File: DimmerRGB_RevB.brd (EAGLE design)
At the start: 75 x 65 mm, 61 parts, among them CON1 CON_10X200MIL, CON2 CON_5X100MIL, IC1 PIC16F18325, IC2 LM2931_ADJ, IC3 LM5111, IC4 LM5111, IC5 74HC14D, Q2 N-PWR-MOSFETLFPAK, Q3 N-PWR-MOSFETLFPAK, Q4 N-PWR-MOSFETLFPAK, Q5 N-PWR-MOSFETLFPAK, SW1 PEC11R, SW2 PEC11R, SW3 PEC09, SW4 PEC09

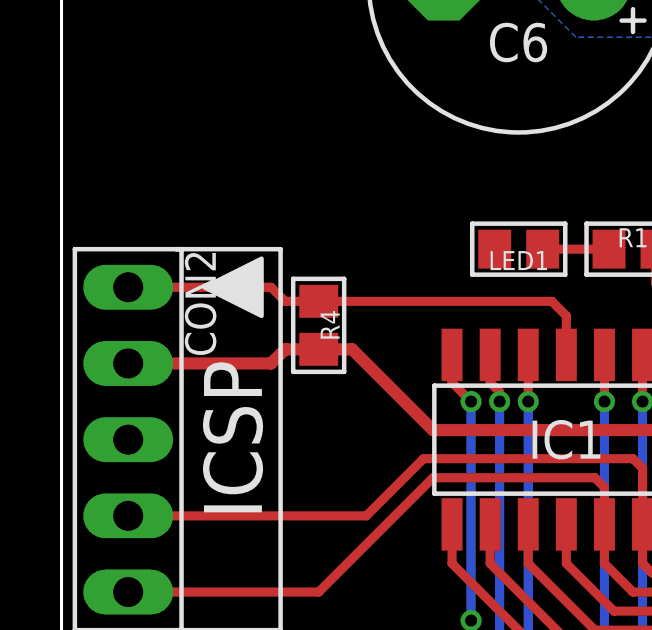
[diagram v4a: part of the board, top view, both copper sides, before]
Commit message: Linear regulator changed
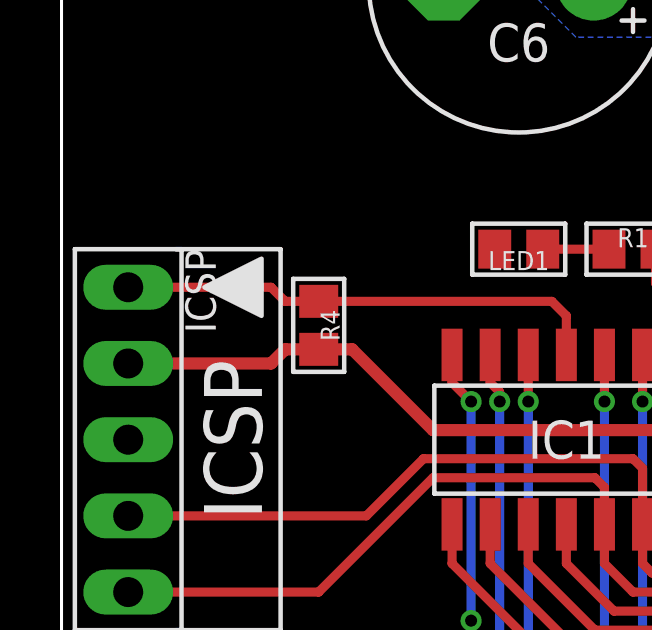
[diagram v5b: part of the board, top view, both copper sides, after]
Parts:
- C3, C4, C5, C6, C7: value 1500u -> 330u 35V
- IC2: value LM2931_ADJ -> LM2936
- IC3, IC4: value LM5111 -> LM5111-1M
- Q1: value (none) -> NX3008NBK
- R2: value 33k -> N/A
- R3: value 10k -> N/A
- R5: value 33k -> 22k
- renumbered CON2 to ICSP
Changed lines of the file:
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@@
 <layer number="25" name="tNames" color="7" fill="1" visible="no" active="yes"/>
 <layer number="26" name="bNames" color="7" fill="1" visible="no" active="yes"/>
-<layer number="27" name="tValues" color="7" fill="1" visible="no" active="yes"/>
+<layer number="27" name="tValues" color="7" fill="1" visible="yes" active="yes"/>
 <layer number="28" name="bValues" color="7" fill="1" visible="no" active="yes"/>
 <layer number="29" name="tStop" color="7" fill="3" visible="no" active="yes"/>
@@
 <element name="Q5" library="00Mosfet" package="LFPAK" value="N-PWR-MOSFETLFPAK" x="60.0075" y="36.83" rot="R270"/>
 <element name="Q4" library="00Mosfet" package="LFPAK" value="N-PWR-MOSFETLFPAK" x="49.8475" y="36.83" rot="R270"/>
-<element name="IC4" library="00Logic" package="SOIC8" value="LM5111" x="49.2125" y="29.21" rot="R90"/>
-<element name="IC2" library="00VoltageRegulator" package="SOIC8" value="LM2931_ADJ" x="61.595" y="25.0825" rot="R270"/>
+<element name="IC4" library="00Logic" package="SOIC8" value="LM5111-1M" x="49.2125" y="29.21" rot="R90"/>
+<element name="IC2" library="00VoltageRegulator" package="SOIC8" value="LM2936" x="61.595" y="25.0825" rot="R270"/>
 <element name="C1" library="00Capacitor" package="SMC_C" value="33u" x="66.04" y="25.7175" rot="R270"/>
 <element name="C10" library="00Capacitor" package="C0805" value="100n" x="52.705" y="29.5275" rot="R270"/>
 <element name="Q3" library="00Mosfet" package="LFPAK" value="N-PWR-MOSFETLFPAK" x="39.6875" y="36.83" rot="R270"/>
-<element name="IC3" library="00Logic" package="SOIC8" value="LM5111" x="31.4325" y="29.21" rot="R90"/>
+<element name="IC3" library="00Logic" package="SOIC8" value="LM5111-1M" x="31.4325" y="29.21" rot="R90"/>
 <element name="C9" library="00Capacitor" package="C0805" value="100n" x="34.925" y="29.5275" rot="R270"/>
 <element name="SW1" library="00Switch" package="ENCODER_BOURNS" value="PEC11R" x="20" y="10.5" locked="yes" rot="MR0"/>
@@
 <element name="C16" library="00Capacitor" package="C0805" value="10n" x="40.005" y="2.54" rot="R90"/>
 <element name="CON1" library="00Connector" package="200MIL_10X" value="CON_10X200MIL" x="38.1" y="60.7225"/>
-<element name="C7" library="00Capacitor" package="10MM" value="1500u" x="25.4" y="45.4025" rot="R270"/>
-<element name="C5" library="00Capacitor" package="10MM" value="1500u" x="55.88" y="45.4025" rot="R270"/>
-<element name="C4" library="00Capacitor" package="10MM" value="1500u" x="35.56" y="45.4025" rot="R270"/>
-<element name="C3" library="00Capacitor" package="10MM" value="1500u" x="45.72" y="45.4025" rot="R270"/>
+<element name="C7" library="00Capacitor" package="10MM" value="330u 35V" x="25.4" y="45.4025" rot="R270"/>
+<element name="C5" library="00Capacitor" package="10MM" value="330u 35V" x="55.88" y="45.4025" rot="R270"/>
+<element name="C4" library="00Capacitor" package="10MM" value="330u 35V" x="35.56" y="45.4025" rot="R270"/>
+<element name="C3" library="00Capacitor" package="10MM" value="330u 35V" x="45.72" y="45.4025" rot="R270"/>
 <element name="IC1" library="00PIC" package="SO14" value="PIC16F18325" x="16.8275" y="30.1625" rot="R180"/>
 <element name="Q2" library="00Mosfet" package="LFPAK" value="N-PWR-MOSFETLFPAK" x="29.5275" y="36.83" rot="R270"/>
@@
 <element name="LED1" library="00Display" package="LED0805" value="" x="15.24" y="36.5125" rot="R180"/>
 <element name="R1" library="00Resistor" package="R0805" value="1k" x="19.05" y="36.5125"/>
-<element name="Q1" library="00Mosfet" package="SOT23" value="" x="52.705" y="22.5425" rot="R270"/>
-<element name="R5" library="00Resistor" package="R0805" value="33k" x="61.595" y="20.6375"/>
-<element name="R2" library="00Resistor" package="R0805" value="33k" x="58.1025" y="29.5275" rot="R90"/>
-<element name="R3" library="00Resistor" package="R0805" value="10k" x="58.1025" y="26.035" rot="R90"/>
-<element name="C6" library="00Capacitor" package="10MM" value="1500u" x="15.24" y="45.4025" rot="R180"/>
+<element name="Q1" library="00Mosfet" package="SOT23" value="NX3008NBK" x="52.705" y="22.5425" rot="R270"/>
+<element name="R5" library="00Resistor" package="R0805" value="22k" x="61.595" y="20.6375"/>
+<element name="R2" library="00Resistor" package="R0805" value="N/A" x="58.1025" y="29.5275" rot="R90"/>
+<element name="R3" library="00Resistor" package="R0805" value="N/A" x="58.1025" y="26.035" rot="R90"/>
+<element name="C6" library="00Capacitor" package="10MM" value="330u 35V" x="15.24" y="45.4025" rot="R180"/>
 <element name="D4" library="00Diode" package="SOD323" value="SCHOTTKYSOD323" x="45.72" y="11.1125" rot="R90"/>
 <element name="D2" library="00Diode" package="SOD323" value="SCHOTTKYSOD323" x="56.8325" y="19.685"/>
 <element name="SW3" library="00Switch" package="PEC09" value="PEC09" x="20" y="3" locked="yes"/>
 <element name="SW4" library="00Switch" package="PEC09" value="PEC09" x="55" y="3" locked="yes"/>
-<element name="CON2" library="00Connector" package="100MIL_5X" value="CON_5X100MIL" x="2.2225" y="30.1625" rot="R270"/>
+<element name="ICSP" library="00Connector" package="100MIL_5X" value="CON_5X100MIL" x="2.2225" y="30.1625" rot="R270"/>
 <element name="C8" library="00Capacitor" package="C0805" value="100n" x="65.405" y="20.6375"/>
 <element name="C20" library="00Capacitor" package="C0805" value="100n" x="28.2575" y="5.08" rot="R90"/>
@@
 <via x="41.5925" y="4.7625" extent="1-16" drill="0.6"/>
 <via x="33.3375" y="4.7625" extent="1-16" drill="0.6"/>
-<contactref element="CON2" pad="3"/>
+<contactref element="ICSP" pad="3"/>
 <via x="30.7975" y="29.21" extent="1-16" drill="0.6"/>
 <via x="32.0675" y="29.21" extent="1-16" drill="0.6"/>
@@
 <wire x1="37.465" y1="2.2225" x2="37.465" y2="13.0175" width="0.4064" layer="1"/>
 <wire x1="37.465" y1="13.0175" x2="37.7825" y2="13.335" width="0.4064" layer="1"/>
-<contactref element="CON2" pad="2"/>
+<contactref element="ICSP" pad="2"/>
 <wire x1="2.2225" y1="32.7025" x2="6.985" y2="32.7025" width="0.4064" layer="1"/>
 <wire x1="6.985" y1="32.7025" x2="7.455" y2="33.1725" width="0.4064" layer="1"/>
@@
 <contactref element="R4" pad="1"/>
 <contactref element="IC1" pad="4"/>
-<contactref element="CON2" pad="1"/>
+<contactref element="ICSP" pad="1"/>
 <wire x1="2.2225" y1="35.2425" x2="6.985" y2="35.2425" width="0.3048" layer="1"/>
 <wire x1="6.985" y1="35.2425" x2="7.455" y2="34.7725" width="0.3048" layer="1"/>
@@
 <contactref element="IC1" pad="12"/>
 <contactref element="IC3" pad="2"/>
-<contactref element="CON2" pad="5"/>
+<contactref element="ICSP" pad="5"/>
 <wire x1="30.7975" y1="26.56" x2="30.7975" y2="25.7175" width="0.3048" layer="1"/>
 <wire x1="30.7975" y1="25.7175" x2="30.48" y2="25.4" width="0.3048" layer="1"/>
@@
 <contactref element="IC1" pad="13"/>
 <contactref element="Q1" pad="1"/>
-<contactref element="CON2" pad="4"/>
+<contactref element="ICSP" pad="4"/>
 <via x="50.4825" y="23.495" extent="1-16" drill="0.4"/>
 <via x="47.3075" y="25.0825" extent="1-16" drill="0.4"/>
